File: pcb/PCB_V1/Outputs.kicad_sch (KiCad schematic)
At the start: 18 parts, among them J501 FAN1 / 3.5 mm, J511 FAN2 / 3.5 mm, J521 PUMP + / switched - (3.5 mm), Q501 AO3400A, Q511 AO3400A, Q521 AO3422

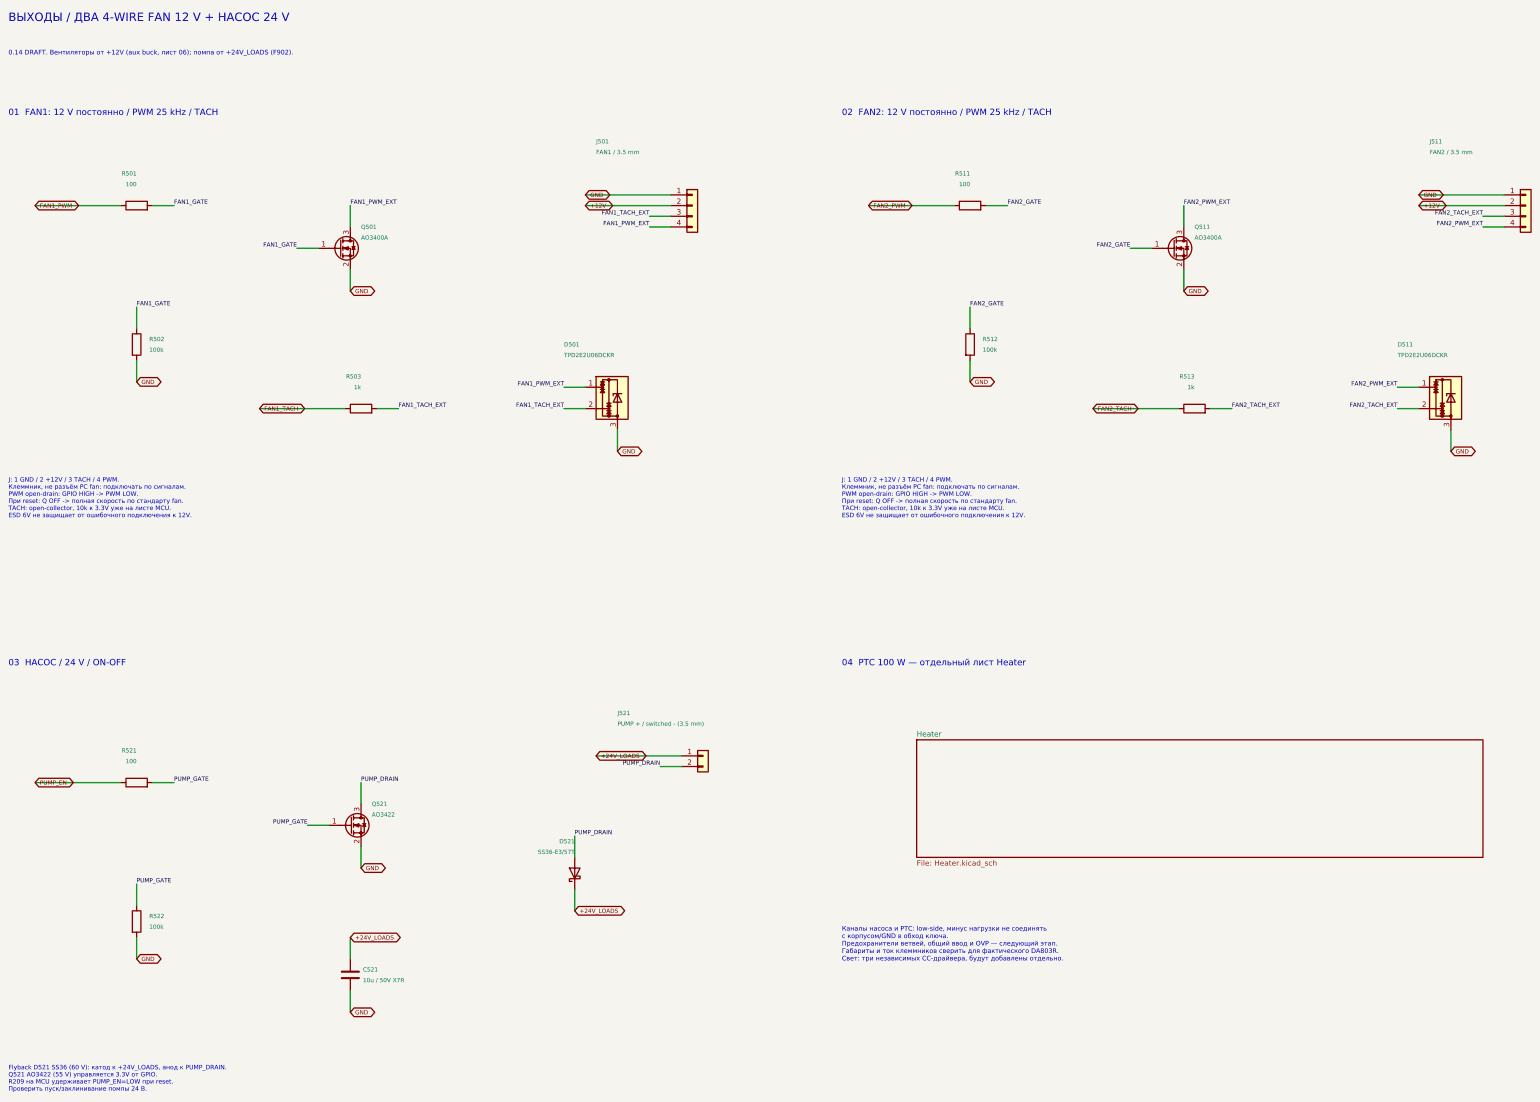
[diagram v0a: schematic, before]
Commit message: pcb: refine 24 V bias, branch protection and auxiliary supply
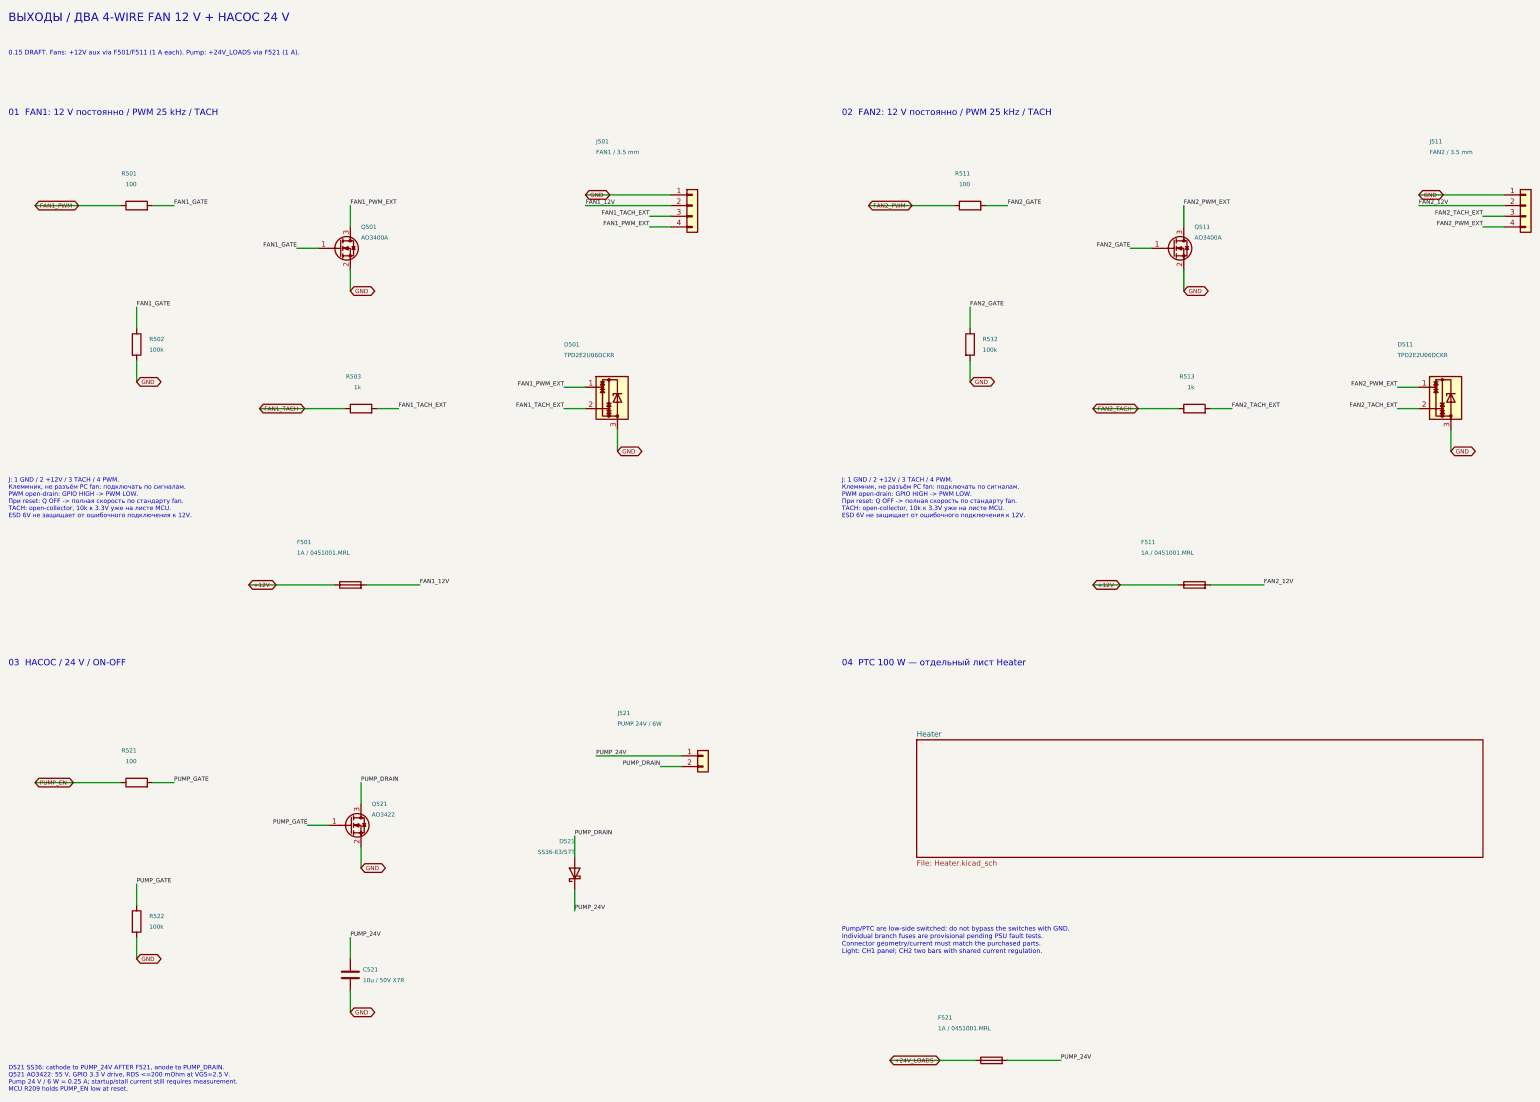
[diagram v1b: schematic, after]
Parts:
- added F501, F511, F521: 1A / 0451001.MRL, GrowBox:Fuse_Littelfuse_451, symbol Device:Fuse
- J521: value PUMP + / switched - (3.5 mm) -> PUMP 24V / 6W
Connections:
- net +12V: now also F501.1, F511.1; no longer J501.2 (Pin_2), J511.2 (Pin_2)
- net +24V_LOADS: now also F521.1; no longer C521.1, D521.1 (K), J521.1 (Pin_1)
- new net FAN1_12V: F501.2, J501.2 (Pin_2)
- new net FAN2_12V: F511.2, J511.2 (Pin_2)
- new net PUMP_24V: C521.1, D521.1 (K), F521.2, J521.1 (Pin_1)
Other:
- note added: "0.15 DRAFT. Fans: +12V aux via F501/F511 (1 A each). Pump: +24V_LOADS via F521 (1 A)."
- note added: "D521 SS36: cathode to PUMP_24V AFTER F521, anode to PUMP_DRAIN. Q521 AO3422: 55 V, GPIO 3.3 V drive, RDS <=200 mOhm at VGS=2.5 V. Pump 24 V / 6 W = 0.25 A; startup/stall current still requires measurement. MCU R209 holds PUMP_EN low at reset."
- note added: "Pump/PTC are low-side switched: do not bypass the switches with GND. Individual branch fuses are provisional pending PSU fault tests. Connector geometry/current must match the purchased parts. Light: CH1 panel; CH2 two bars with shared current regulation."
- note removed: "0.14 DRAFT. Вентиляторы от +12V (aux buck, лист 06); помпа от +24V_LOADS (F902)."
- note removed: "Flyback D521 SS36 (60 V): катод к +24V_LOADS, анод к PUMP_DRAIN. Q521 AO3422 (55 V) управляется 3.3V от GPIO. R209 на MCU удерживает PUMP_EN=LOW при reset. Проверить пуск/заклинивание помпы 24 В."
- note removed: "Каналы насоса и PTC: low-side, минус нагрузки не соединять с корпусом/GND в обход ключа. Предохранители ветвей, общий ввод и OVP — следующий этап. Габариты и ток клеммников сверить для фактического DA803R. Свет: три независимых CC-драйвера, будут добавлены отдельно."
